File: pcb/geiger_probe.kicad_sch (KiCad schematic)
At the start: 0 parts

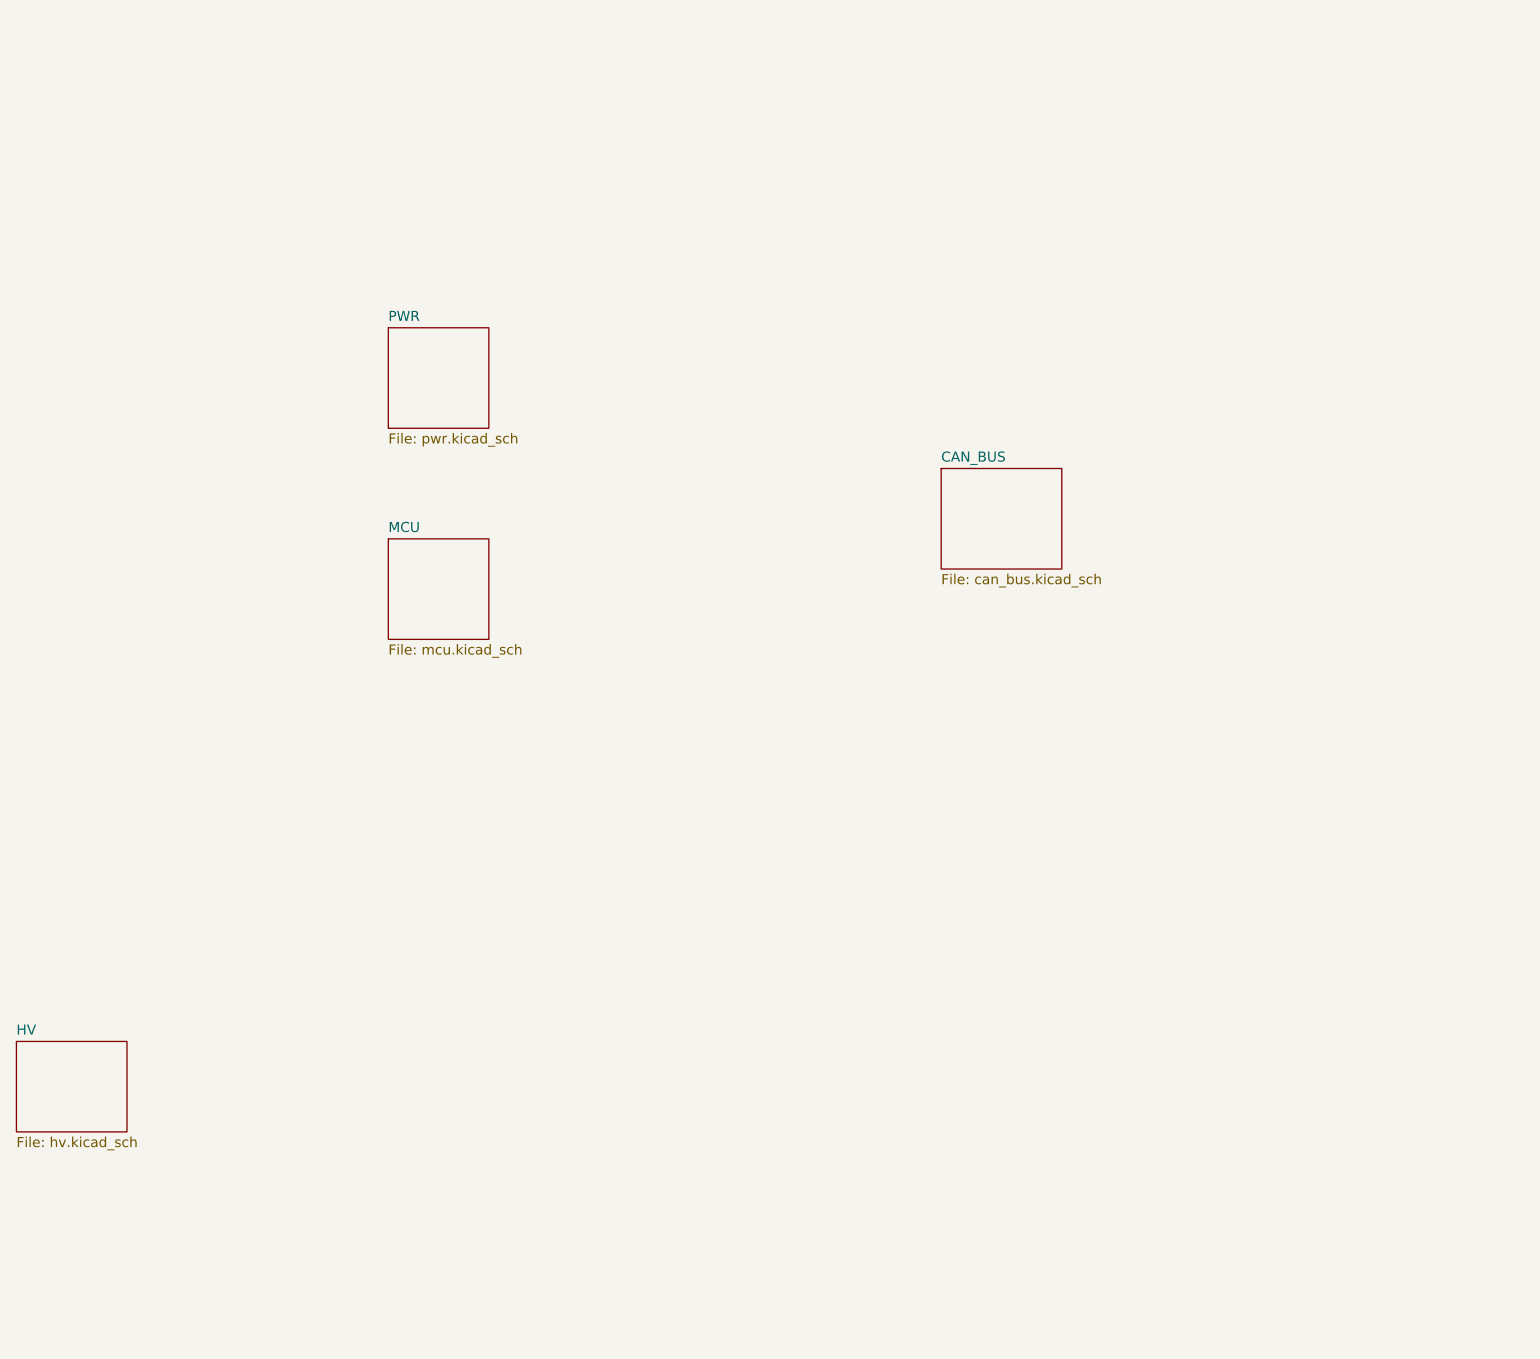
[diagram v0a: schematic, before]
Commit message: Sch almost done, maybe add current sense
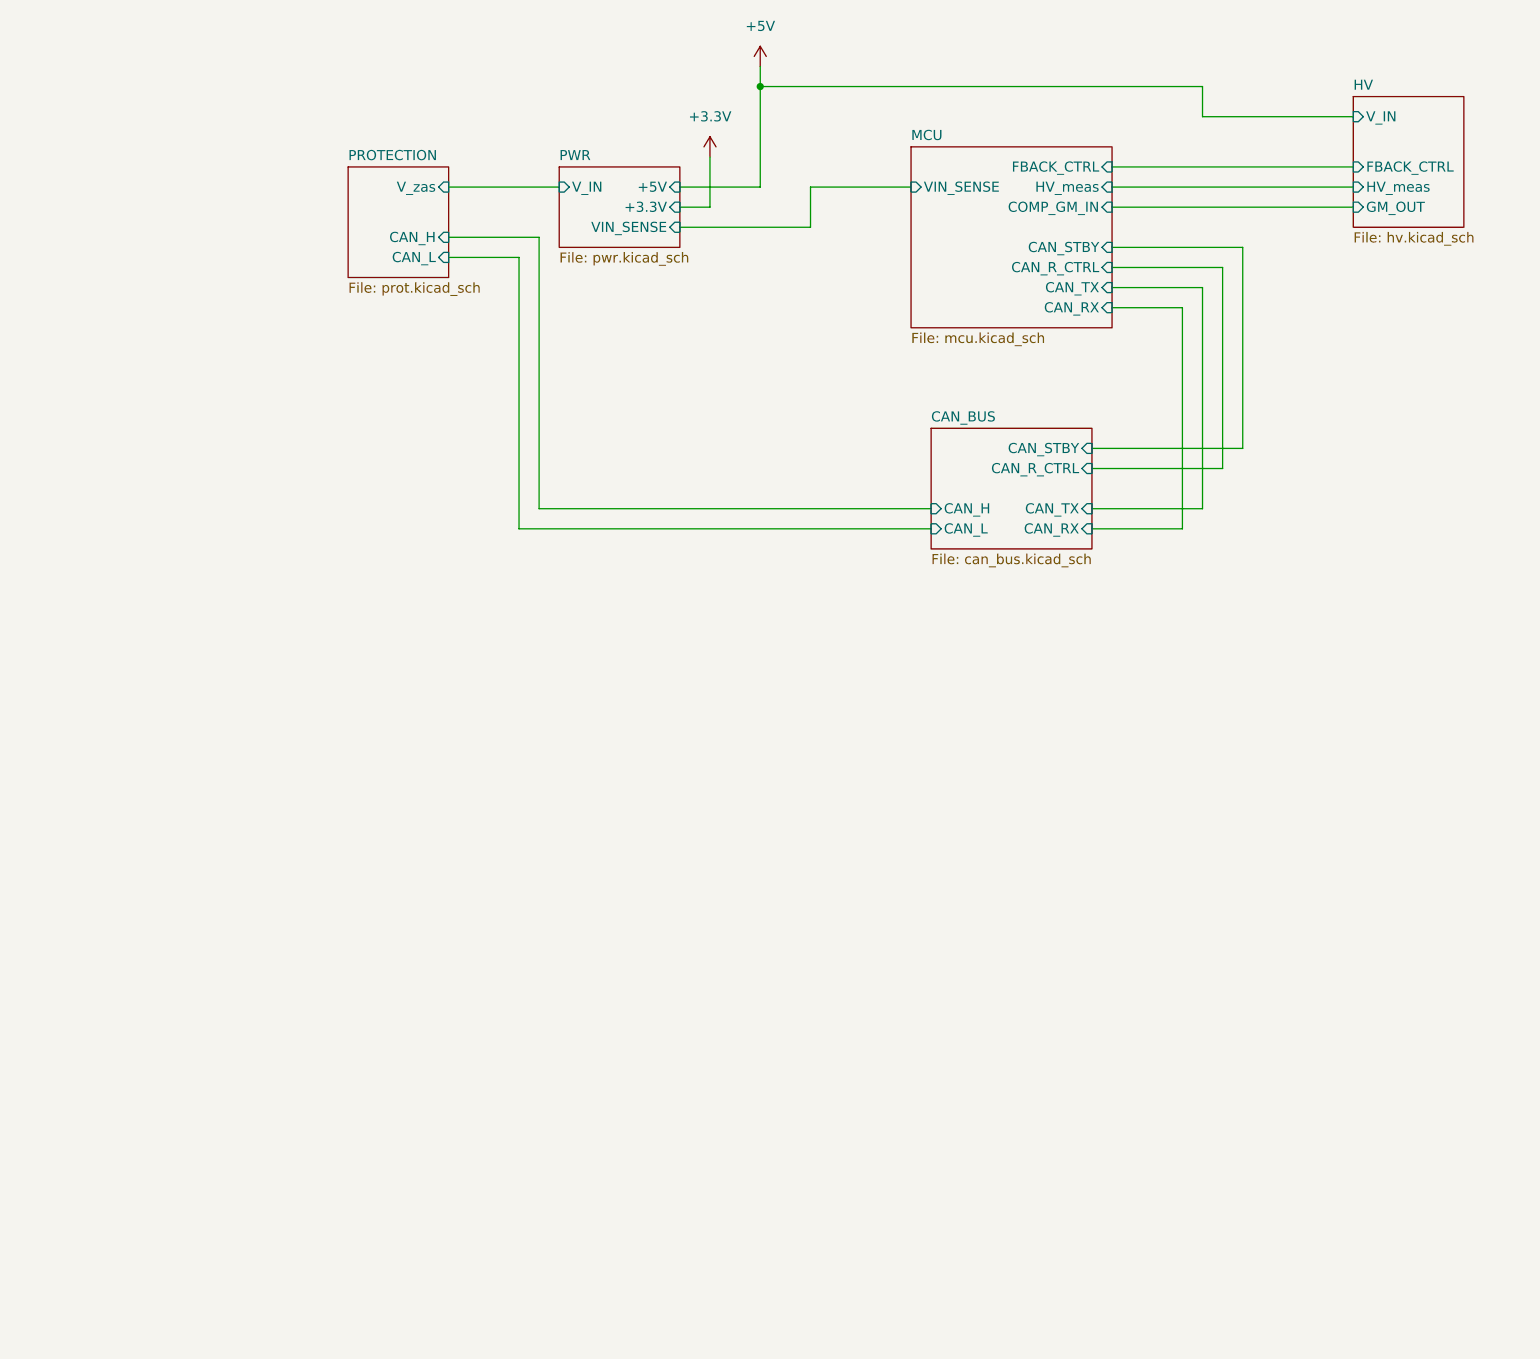
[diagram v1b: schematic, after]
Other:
- added sheet PROTECTION (prot.kicad_sch)
- sheet CAN_BUS ports: added CAN_H, CAN_L, CAN_RX, CAN_R_CTRL, CAN_STBY, CAN_TX; removed none
- sheet HV ports: added FBACK_CTRL, GM_OUT, HV_meas, V_IN; removed none
- sheet MCU ports: added CAN_RX, CAN_R_CTRL, CAN_STBY, CAN_TX, COMP_GM_IN, FBACK_CTRL, HV_meas, VIN_SENSE; removed none
- sheet PWR ports: added +3.3V, +5V, VIN_SENSE, V_IN; removed none

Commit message: Scheamtic almost finished, astarted firmware and pcb
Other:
- sheet HV ports: added +5V, COMP_GM; removed GM_OUT, V_IN
- sheet MCU ports: added COMP_GM, EN_I_SENS, I_SENS; removed COMP_GM_IN
- sheet PWR ports: added EN_I_SENS, I_SENS; removed none
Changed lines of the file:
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@@
+	(wire
+		(pts
+			(xy 130.81 58.42) (xy 160.02 58.42)
+		)
+		(stroke
+			(width 0)
+			(type default)
+		)
+	)
 	(wire
 		(pts
@@
 	(wire
 		(pts
-			(xy 147.32 49.53) (xy 160.02 49.53)
-		)
-		(stroke
-			(width 0)
-			(type default)
-		)
-	)
-	(wire
-		(pts
 			(xy 134.62 52.07) (xy 130.81 52.07)
 		)
@@
 	(wire
 		(pts
-			(xy 130.81 54.61) (xy 147.32 54.61)
+			(xy 130.81 55.88) (xy 160.02 55.88)
 		)
 		(stroke
@@
 	(wire
 		(pts
-			(xy 147.32 54.61) (xy 147.32 49.53)
+			(xy 130.81 60.96) (xy 160.02 60.96)
 		)
 		(stroke
@@
 			)
 		)
-		(pin "CAN_R_CTRL" input
+		(pin "CAN_R_CTRL" output
 			(at 185.42 59.69 0)
 			(effects
@@
 			)
 		)
-		(pin "CAN_STBY" input
+		(pin "CAN_STBY" output
 			(at 185.42 57.15 0)
 			(effects
@@
 			)
 		)
-		(pin "CAN_TX" input
+		(pin "CAN_TX" output
 			(at 185.42 62.23 0)
 			(effects
@@
 			)
 		)
-		(pin "COMP_GM_IN" input
+		(pin "COMP_GM" input
 			(at 185.42 52.07 0)
 			(effects
@@
 			)
 		)
-		(pin "FBACK_CTRL" input
+		(pin "FBACK_CTRL" output
 			(at 185.42 46.99 0)
 			(effects
@@
 		)
 		(pin "VIN_SENSE" input
-			(at 160.02 49.53 180)
+			(at 160.02 55.88 180)
+			(effects
+				(font
+					(size 1.27 1.27)
+				)
+				(justify left)
+			)
+		)
+		(pin "I_SENS" input
+			(at 160.02 58.42 180)
+			(effects
+				(font
+					(size 1.27 1.27)
+				)
+				(justify left)
+			)
+		)
+		(pin "EN_I_SENS" output
+			(at 160.02 60.96 180)
 			(effects
 				(font
@@
 			)
 		)
-		(pin "CAN_H" input
+		(pin "CAN_H" bidirectional
 			(at 101.6 55.88 0)
 			(effects
@@
 			)
 		)
-		(pin "CAN_L" input
+		(pin "CAN_L" bidirectional
 			(at 101.6 58.42 0)
 			(effects
@@
 			)
 		)
-		(pin "V_zas" input
+		(pin "V_zas" output
 			(at 101.6 49.53 0)
 			(effects
@@
 			)
 		)
-		(pin "GM_OUT" input
+		(pin "COMP_GM" output
 			(at 215.9 52.07 180)
 			(effects
@@
 			)
 		)
-		(pin "HV_meas" input
+		(pin "HV_meas" output
 			(at 215.9 49.53 180)
 			(effects
@@
 			)
 		)
-		(pin "V_IN" input
+		(pin "+5V" input
 			(at 215.9 40.64 180)
 			(effects
@@
 			)
 		)
-		(pin "CAN_H" input
+		(pin "CAN_H" bidirectional
 			(at 162.56 90.17 180)
 			(effects
@@
 			)
 		)
-		(pin "CAN_L" input
+		(pin "CAN_L" bidirectional
 			(at 162.56 92.71 180)
 			(effects
@@
 			)
 		)
-		(pin "CAN_RX" input
+		(pin "CAN_RX" output
 			(at 182.88 92.71 0)
 			(effects
@@
 	(sheet
 		(at 115.57 46.99)
-		(size 15.24 10.16)
+		(size 15.24 16.51)
 		(exclude_from_sim no)
 		(in_bom yes)
@@
 		)
 		(property "Sheetfile" "pwr.kicad_sch"
-			(at 115.57 57.7346 0)
+			(at 115.57 64.0846 0)
 			(show_name no)
 			(do_not_autoplace no)
@@
 			)
 		)
-		(pin "+3.3V" input
+		(pin "+3.3V" output
 			(at 130.81 52.07 0)
 			(effects
@@
 			)
 		)
-		(pin "+5V" input
+		(pin "+5V" output
 			(at 130.81 49.53 0)
 			(effects
@@
 			)
 		)
-		(pin "VIN_SENSE" input
-			(at 130.81 54.61 0)
-			(effects
-				(font
+		(pin "VIN_SENSE" output
+			(at 130.81 55.88 0)
+			(effects
+				(font
+					(size 1.27 1.27)
+				)
+				(justify right)
+			)
+		)
+		(pin "EN_I_SENS" input
+			(at 130.81 60.96 0)
+			(effects
+				(font
+					(size 1.27 1.27)
+				)
+				(justify right)
+			)
+		)
+		(pin "I_SENS" output
+			(at 130.81 58.42 0)
+			(effects
+				(font

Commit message: Add J1 net labels and fiducials, regenerate production outputs
- Named nets on J1 pads (schematic + PCB)
- 2 fiducials for stencil alignment (hand assembly)
- Regenerate PDFs, gerber zip, interactive BOM and 3D renders
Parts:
- added FID1, FID2: Fiducial, Fiducial:Fiducial_0.5mm_Mask1mm, symbol Mechanical:Fiducial
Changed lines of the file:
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@@
+	)
+	(symbol
+		(lib_id "Mechanical:Fiducial")
+		(at 162.56 193.04 0)
+		(unit 1)
+		(body_style 1)
+		(exclude_from_sim no)
+		(in_bom no)
+		(on_board yes)
+		(in_pos_files yes)
+		(dnp no)
+		(fields_autoplaced yes)
+		(property "Reference" "FID1"
+			(at 165.1 191.7699 0)
+			(show_name no)
+			(do_not_autoplace no)
+			(effects
+				(font
+					(size 1.27 1.27)
+				)
+				(justify left)
+			)
+		)
+		(property "Value" "Fiducial"
+			(at 165.1 194.3099 0)
+			(show_name no)
+			(do_not_autoplace no)
+			(effects
+				(font
+					(size 1.27 1.27)
+				)
+				(justify left)
+			)
+		)
+		(property "Footprint" "Fiducial:Fiducial_0.5mm_Mask1mm"
+			(at 162.56 193.04 0)
+			(hide yes)
+			(show_name no)
+			(do_not_autoplace no)
+			(effects
+				(font
+					(size 1.27 1.27)
+				)
+			)
+		)
+		(property "Datasheet" ""
+			(at 162.56 193.04 0)
+			(hide yes)
+			(show_name no)
+			(do_not_autoplace no)
+			(effects
+				(font
+					(size 1.27 1.27)
+				)
+			)
+		)
+		(property "Description" "Fiducial Marker"
+			(at 162.56 193.04 0)
+			(hide yes)
+			(show_name no)
+			(do_not_autoplace no)
+			(effects
+				(font
+					(size 1.27 1.27)
+				)
+			)
+		)
+		(instances
+			(project "geiger_probe"
+				(path "/eb6e66b6-2df0-4872-8f92-4c510b34f8fe"
+					(reference "FID1")
+					(unit 1)
+				)
+			)
+		)
 	)
 	(symbol
@@
 					(unit 1)
 				)
+			)
+		)
+	)
+	(symbol
+		(lib_id "Mechanical:Fiducial")
+		(at 162.56 187.96 0)
+		(unit 1)
+		(body_style 1)
+		(exclude_from_sim no)
+		(in_bom no)
+		(on_board yes)
+		(in_pos_files yes)
+		(dnp no)
+		(fields_autoplaced yes)
+		(property "Reference" "FID2"
+			(at 165.1 186.6899 0)
+			(show_name no)
+			(do_not_autoplace no)
+			(effects
+				(font
+					(size 1.27 1.27)
+				)
+				(justify left)
+			)
+		)
+		(property "Value" "Fiducial"
+			(at 165.1 189.2299 0)
+			(show_name no)
+			(do_not_autoplace no)
+			(effects
+				(font
+					(size 1.27 1.27)
+				)
+				(justify left)
+			)
+		)
+		(property "Footprint" "Fiducial:Fiducial_0.5mm_Mask1mm"
+			(at 162.56 187.96 0)
+			(hide yes)
+			(show_name no)
+			(do_not_autoplace no)
+			(effects
+				(font
+					(size 1.27 1.27)
+				)
+			)
+		)
+		(property "Datasheet" ""
+			(at 162.56 187.96 0)
+			(hide yes)
+			(show_name no)
+			(do_not_autoplace no)
+			(effects
+				(font
+					(size 1.27 1.27)
+				)
+			)
+		)
+		(property "Description" "Fiducial Marker"
+			(at 162.56 187.96 0)
+			(hide yes)
+			(show_name no)
+			(do_not_autoplace no)
+			(effects
+				(font
+					(size 1.27 1.27)
+				)
+			)
+		)
+		(instances
+			(project "geiger_probe"
+				(path "/eb6e66b6-2df0-4872-8f92-4c510b34f8fe"
+					(reference "FID2")
+					(unit 1)
+				)
